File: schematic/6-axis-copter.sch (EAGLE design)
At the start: 89 parts

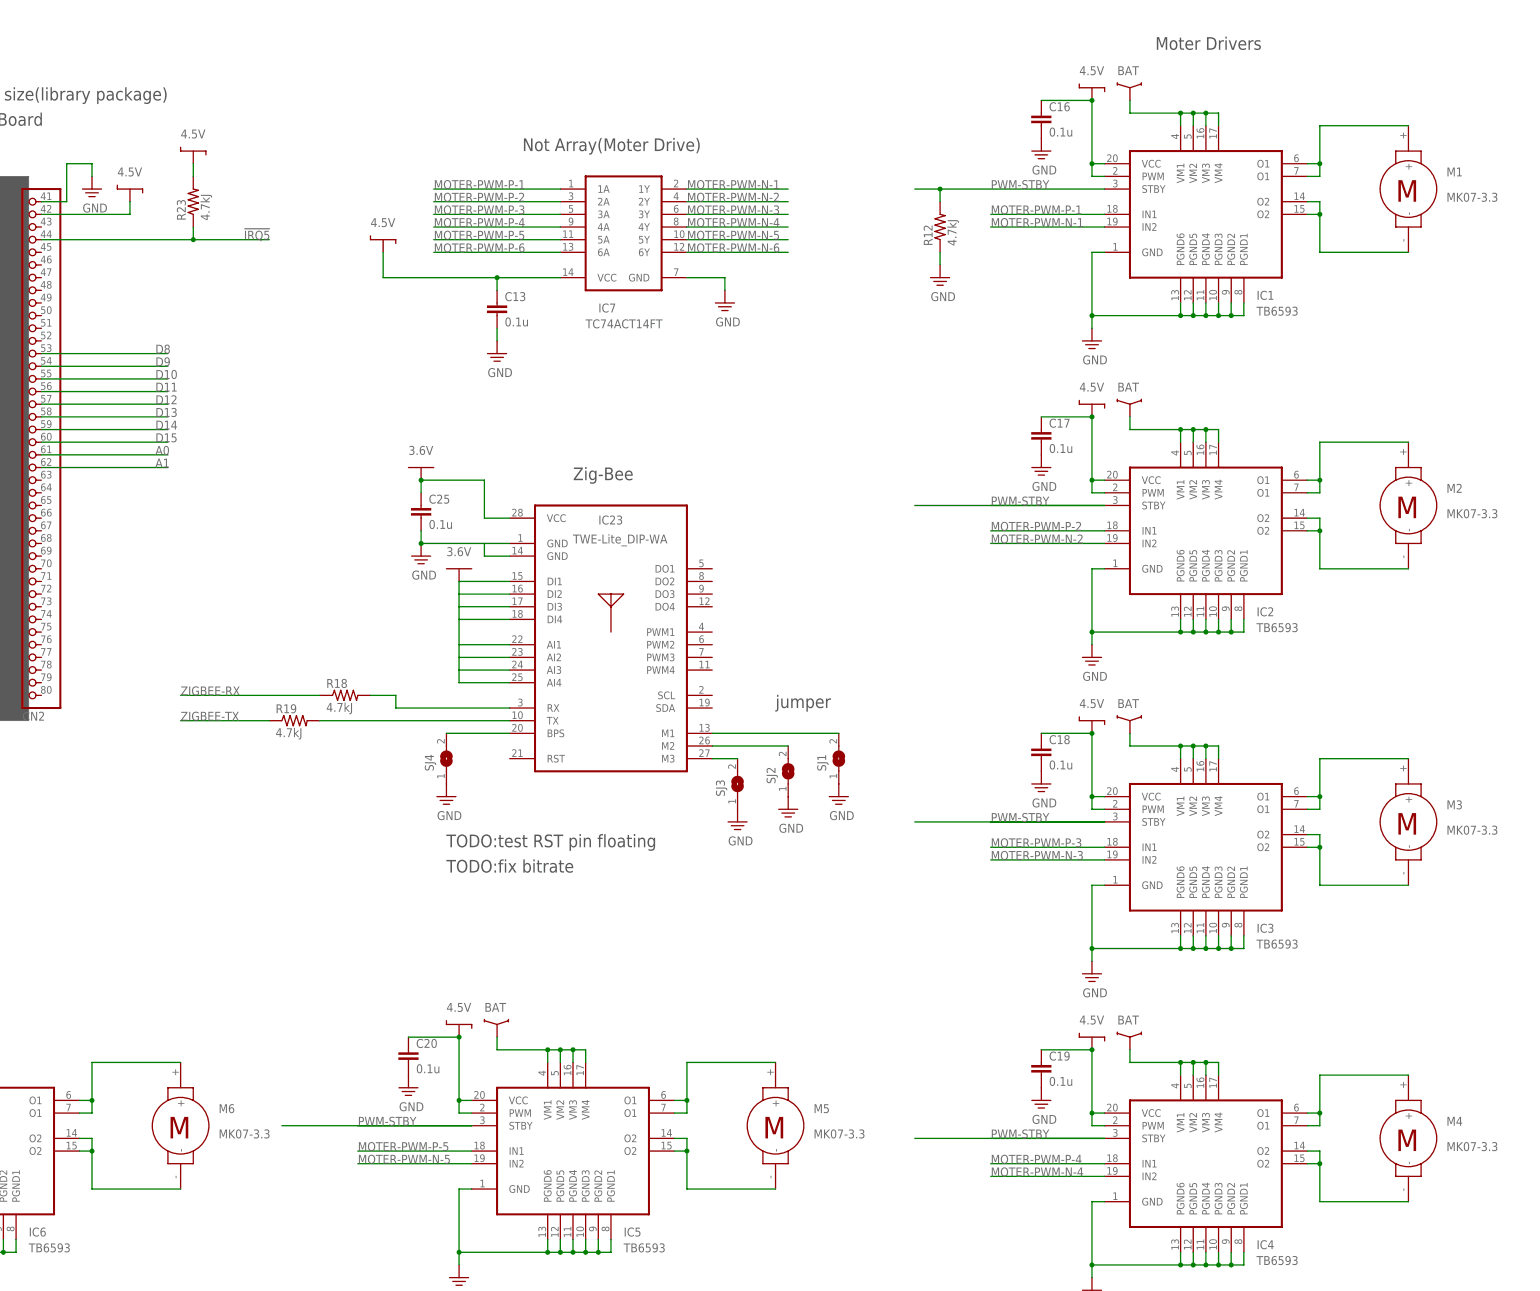
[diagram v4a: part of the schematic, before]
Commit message: 回路図のモーターに直列にコイル追加
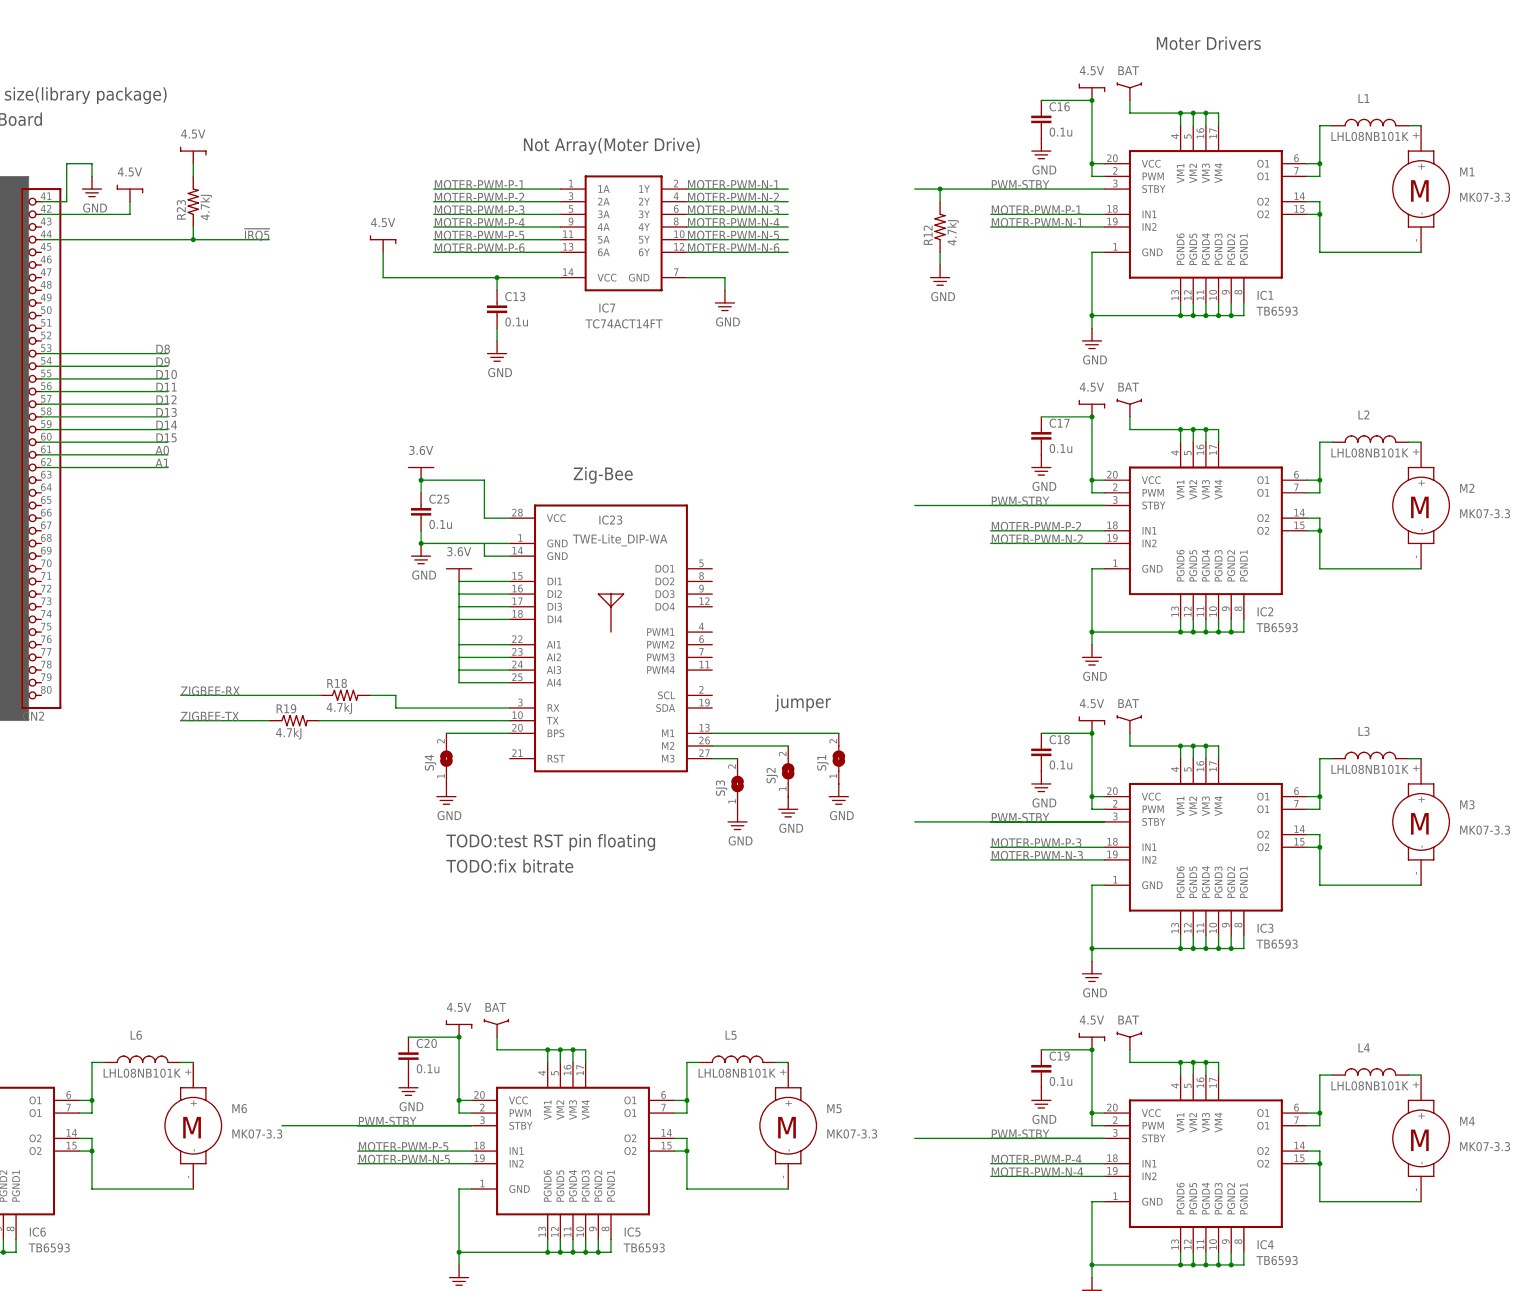
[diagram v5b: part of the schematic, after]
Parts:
- added L1, L2, L3, L4, L5, L6: LHL08NB101K, passive:LHL08
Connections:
- new net N$13: L1.2, M1.+
- new net N$25: L2.2, M2.+
- new net N$26: L3.2, M3.+
- new net N$27: L4.2, M4.+
- new net N$35: L5.2, M5.+
- new net N$38: L6.2, M6.+
- net N$1: now also L1.1; no longer M1.+
- net N$11: now also L6.1; no longer M6.+
- net N$3: now also L2.1; no longer M2.+
- net N$5: now also L3.1; no longer M3.+
- net N$7: now also L4.1; no longer M4.+
- net N$9: now also L5.1; no longer M5.+
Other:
- moved on the sheet: M1, M2, M3, M4, M5, M6

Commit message: 回路図にバッテリーSW追加
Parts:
- added SW1: SS12D01G4, SW:SS12D01G4
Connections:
- new net N$39: F1.1, SW1.3
- net N$23: now also SW1.1, SW1.2; no longer F1.1
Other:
- note added: "SW"
- note removed: "TODO:check board size(library package)"
- note removed: "TODO:fix bitrate"
- note removed: "TODO:insert connector"
- note removed: "TODO:test RST pin floating"
- moved on the sheet: B1, D1, F1
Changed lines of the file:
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@@
 <setting verticaltext="up"/>
 </settings>
-<grid distance="0.1" unitdist="inch" unit="inch" style="lines" multiple="1" display="yes" altdistance="0.01" altunitdist="inch" altunit="inch"/>
+<grid distance="0.1" unitdist="inch" unit="inch" style="lines" multiple="1" display="no" altdistance="0.01" altunitdist="inch" altunit="inch"/>
 <layers>
 <layer number="1" name="Top" color="4" fill="1" visible="no" active="no"/>
@@
 <part name="L5" library="passive" deviceset="LHL08" device="" value="LHL08NB101K"/>
 <part name="L6" library="passive" deviceset="LHL08" device="" value="LHL08NB101K"/>
+<part name="SW1" library="SW" deviceset="SS12D01G4" device="" value="SS12D01G4"/>
 </parts>
 <sheets>
@@
 <text x="200.66" y="99.06" size="2.54" layer="97" font="vector">4.5V Regulator</text>
 <text x="198.12" y="50.8" size="2.54" layer="97" font="vector">3.6V Regulator</text>
-<text x="30.48" y="99.06" size="2.54" layer="97" font="vector">Battery</text>
+<text x="22.86" y="86.36" size="2.54" layer="97" font="vector">Battery</text>
 <text x="25.4" y="289.56" size="2.54" layer="97" font="vector">Distance Sensor</text>
 <text x="104.14" y="251.46" size="2.54" layer="97" font="vector">Acceleration Sensor 3</text>
@@
 <text x="449.58" y="261.62" size="2.54" layer="97" font="vector">Not Array(Moter Drive)</text>
 <text x="500.38" y="149.86" size="2.54" layer="97" font="vector">jumper</text>
-<text x="434.34" y="116.84" size="2.54" layer="97" font="vector">TODO:fix bitrate</text>
-<text x="33.02" y="109.22" size="2.54" layer="97" font="vector">TODO:insert connector</text>
-<text x="434.34" y="121.92" size="2.54" layer="97" font="vector">TODO:test RST pin floating</text>
 <text x="459.74" y="195.58" size="2.54" layer="97" font="vector">Zig-Bee</text>
 <polygon width="0.1524" layer="97" spacing="12.7">
@@
 </polygon>
 <text x="332.74" y="266.7" size="2.54" layer="97" font="vector">H8 Pro Board</text>
-<text x="314.96" y="271.78" size="2.54" layer="97" font="vector">TODO:check board size(library package)</text>
+<text x="33.02" y="111.76" size="2.54" layer="97" font="vector">SW</text>
 </plain>
 <instances>
@@
 <instance part="P+18" gate="G$1" x="60.96" y="180.34"/>
 <instance part="P+19" gate="G$1" x="60.96" y="154.94"/>
-<instance part="SUPPLY14" gate="PE" x="40.64" y="68.58"/>
+<instance part="SUPPLY14" gate="PE" x="17.78" y="68.58"/>
 <instance part="P+20" gate="G$1" x="144.78" y="101.6"/>
 <instance part="IC14" gate="G$1" x="210.82" y="81.28"/>
@@
 <instance part="R7" gate="G$1" x="96.52" y="96.52"/>
 <instance part="IC21" gate="G$1" x="119.38" y="73.66"/>
-<instance part="D1" gate="G$1" x="76.2" y="96.52"/>
+<instance part="D1" gate="G$1" x="78.74" y="96.52"/>
 <instance part="SUPPLY27" gate="PE" x="134.62" y="50.8"/>
 <instance part="R8" gate="G$1" x="106.68" y="86.36" rot="R90"/>
 <instance part="R9" gate="G$1" x="139.7" y="66.04" rot="R90"/>
-<instance part="F1" gate="G$1" x="55.88" y="96.52"/>
+<instance part="F1" gate="G$1" x="60.96" y="96.52"/>
 <instance part="P+31" gate="G$1" x="114.3" y="43.18"/>
 <instance part="R10" gate="G$1" x="124.46" y="33.02" rot="R180"/>
@@
 <instance part="P+32" gate="G$1" x="383.54" y="261.62"/>
 <instance part="R23" gate="G$1" x="383.54" y="251.46" rot="R90"/>
-<instance part="B1" gate="G$1" x="40.64" y="78.74" rot="R90"/>
+<instance part="B1" gate="G$1" x="17.78" y="78.74" rot="R90"/>
 <instance part="L1" gate="G$1" x="619.76" y="266.7" smashed="yes" rot="R90">
 <attribute name="NAME" x="619.76" y="273.05" size="1.778" layer="95" rot="R180"/>
@@
 <attribute name="NAME" x="373.38" y="85.09" size="1.778" layer="95" rot="R180"/>
 <attribute name="VALUE" x="381" y="77.47" size="1.778" layer="96" rot="R180"/>
+</instance>
+<instance part="SW1" gate="G$1" x="35.56" y="96.52" smashed="yes">
+<attribute name="NAME" x="39.37" y="101.6" size="1.778" layer="95"/>
+<attribute name="VALUE" x="31.75" y="91.44" size="1.778" layer="95"/>
 </instance>
 </instances>
@@
 <segment>
 <pinref part="SUPPLY14" gate="PE" pin="GND"/>
-<wire x1="40.64" y1="73.66" x2="40.64" y2="71.12" width="0.1524" layer="91"/>
+<wire x1="17.78" y1="73.66" x2="17.78" y2="71.12" width="0.1524" layer="91"/>
 <pinref part="B1" gate="G$1" pin="-"/>
 </segment>
@@
 <wire x1="91.44" y1="96.52" x2="88.9" y2="96.52" width="0.1524" layer="91"/>
 <pinref part="IC21" gate="G$1" pin="IN-"/>
-<wire x1="88.9" y1="96.52" x2="78.74" y2="96.52" width="0.1524" layer="91"/>
+<wire x1="88.9" y1="96.52" x2="81.28" y2="96.52" width="0.1524" layer="91"/>
 <wire x1="106.68" y1="71.12" x2="88.9" y2="71.12" width="0.1524" layer="91"/>
 <wire x1="88.9" y1="71.12" x2="88.9" y2="96.52" width="0.1524" layer="91"/>
@@
 <pinref part="F1" gate="G$1" pin="2"/>
 <pinref part="D1" gate="G$1" pin="A"/>
-<wire x1="63.5" y1="96.52" x2="73.66" y2="96.52" width="0.1524" layer="91"/>
+<wire x1="68.58" y1="96.52" x2="76.2" y2="96.52" width="0.1524" layer="91"/>
 </segment>
 </net>
 <net name="N$23" class="0">
 <segment>
-<pinref part="F1" gate="G$1" pin="1"/>
-<wire x1="50.8" y1="96.52" x2="40.64" y2="96.52" width="0.1524" layer="91"/>
-<wire x1="40.64" y1="96.52" x2="40.64" y2="93.98" width="0.1524" layer="91"/>
+<wire x1="17.78" y1="96.52" x2="17.78" y2="93.98" width="0.1524" layer="91"/>
 <pinref part="B1" gate="G$1" pin="+"/>
+<wire x1="17.78" y1="96.52" x2="20.32" y2="96.52" width="0.1524" layer="91"/>
+<wire x1="35.56" y1="106.68" x2="17.78" y2="106.68" width="0.1524" layer="91"/>
+<wire x1="17.78" y1="106.68" x2="17.78" y2="96.52" width="0.1524" layer="91"/>
+<pinref part="SW1" gate="G$1" pin="1"/>
+<pinref part="SW1" gate="G$1" pin="2"/>
 </segment>
 </net>
@@
 </segment>
 </net>
+<net name="N$39" class="0">
+<segment>
+<pinref part="F1" gate="G$1" pin="1"/>
+<wire x1="50.8" y1="96.52" x2="55.88" y2="96.52" width="0.1524" layer="91"/>
+<pinref part="SW1" gate="G$1" pin="3"/>
+</segment>
+</net>

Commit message: PCBボード図作成
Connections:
- net !IRQ5: no longer IC19.!INT
- net 3.6V: now also IC23.RST
- net MOTER-PWM-N-3: now also IC7.4Y; no longer IC7.3Y
- net MOTER-PWM-N-4: now also IC7.3Y; no longer IC7.4Y
- net MOTER-PWM-P-3: now also IC7.4A; no longer IC7.3A
- net MOTER-PWM-P-4: now also IC7.3A; no longer IC7.4A
